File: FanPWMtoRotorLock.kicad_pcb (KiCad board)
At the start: 2 copper layers, 23 parts, among them J1 0022232031, J2 0022232031, J3 0022232031, J4 0022232031, Q1 2N2907A, Q2 2N2222A, Q3 2N2907A, Q4 2N2222A, U1 NE556

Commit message: Inital board layout work
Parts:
- removed C2: 10uf, Capacitor_THT:CP_Radial_D5.0mm_P2.50mm
- removed J3, J4: 0022232031, digikey-footprints:PinHeader_1x3_P2.54mm_Drill1.02mm
- removed Q1: 2N2907A, Package_TO_SOT_THT:TO-92
- removed Q4: 2N2222A, Package_TO_SOT_THT:TO-92
- removed R10, R11, R12, R7, R8: 10K, Resistor_THT:R_Axial_DIN0309_L9.0mm_D3.2mm_P2.54mm_Vertical
- removed R9: 100, Resistor_THT:R_Axial_DIN0309_L9.0mm_D3.2mm_P2.54mm_Vertical
- C1: footprint Capacitor_THT:CP_Radial_D5.0mm_P2.50mm -> Capacitor_SMD:C_0805_2012Metric_Pad1.18x1.45mm_HandSolder
- J2: footprint digikey-footprints:PinHeader_1x3_P2.54mm_Drill1.02mm -> Connector_JST:JST_PH_B3B-PH-K_1x03_P2.00mm_Vertical
- Q2: value 2N2222A -> MMBT2222A-7-F; footprint Package_TO_SOT_THT:TO-92 -> digikey-footprints:SOT-23-3
- Q3: value 2N2907A -> MMBT2907ALT1G; footprint Package_TO_SOT_THT:TO-92 -> digikey-footprints:SOT-23-3
- R1: footprint Resistor_THT:R_Axial_DIN0309_L9.0mm_D3.2mm_P2.54mm_Vertical -> Resistor_SMD:R_0805_2012Metric_Pad1.20x1.40mm_HandSolder; moved to B.Cu
- R2, R3, R4, R5, R6: footprint Resistor_THT:R_Axial_DIN0309_L9.0mm_D3.2mm_P2.54mm_Vertical -> Resistor_SMD:R_0805_2012Metric_Pad1.20x1.40mm_HandSolder
- U1: value NE556 -> NE555P; footprint Package_DIP:DIP-14_W7.62mm -> Package_SO:SOIC-8_3.9x4.9mm_P1.27mm; moved to B.Cu
- moved R6 86.3 mm to (129.6, 88.1), turned to 90 degrees
- moved R3 74.6 mm to (126.7, 88.1), turned to 90 degrees
- moved Q3 54.3 mm to (131.5, 83.5), turned to 0 degrees
- moved R4 49.1 mm to (129.7, 78.5), turned to 90 degrees
- moved C1 26.4 mm to (132.2, 78.5)
- moved U1 24.3 mm to (129.6, 83.2), turned to 180 degrees
- moved J2 23.5 mm to (119.0, 86.6), turned to 0 degrees
- moved J1 21.7 mm to (118.5, 80.0), turned to 0 degrees
- moved Q2 20.1 mm to (127.7, 83.5), turned to 180 degrees
- moved R5 15.7 mm to (132.4, 88.1), turned to 90 degrees
- moved R1 9.40 mm to (122.3, 82.8)
- moved R2 9.25 mm to (126.8, 78.5), turned to 90 degrees
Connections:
- C1 pad 1: Net-(Q1-C) -> Net-(Q3-E)
- C1 pad 2: Net-(Q1-E) -> Net-(Q2-E)
- J1 pad 1: Net-(Q1-E) -> Net-(Q2-E)
- J1 pad 2: Net-(U1A-R) -> Net-(U1-R)
- J2 pad 1: Net-(Q1-E) -> Net-(Q2-E)
- J2 pad 2: Net-(U1A-R) -> Net-(U1-R)
- Q2 pad 1: Net-(Q2-C) -> Net-(Q2-B)
- Q2 pad 2: Net-(Q2-B) -> Net-(Q2-E)
- Q2 pad 3: Net-(Q1-E) -> Net-(Q2-C)
- Q3 pad 1: Net-(Q3-C) -> Net-(Q3-B)
- Q3 pad 2: Net-(Q3-B) -> Net-(Q2-E)
- Q3 pad 3: Net-(Q1-E) -> Net-(Q3-E)
- R1 pad 1: Net-(U1A-R) -> Net-(U1-R)
- R2 pad 2: Net-(Q1-B) -> Net-(Q3-B)
- R3 pad 1: Net-(U1A-R) -> Net-(U1-R)
- R3 pad 2: Net-(U1A-DIS) -> Net-(U1-DIS)
- R4 pad 1: Net-(U1A-DIS) -> Net-(U1-DIS)
- R4 pad 2: Net-(Q1-C) -> Net-(Q3-E)
- R5 pad 1: Net-(U1A-Q) -> Net-(U1-Q)
- R6 pad 1: Net-(U1A-R) -> Net-(U1-R)
- U1 pad 1: Net-(U1A-DIS) -> Net-(Q2-E)
- U1 pad 2: Net-(U1A-DIS) -> Net-(Q3-B)
- U1 pad 3: unconnected-(U1A-CV-Pad3) -> Net-(U1-Q)
- U1 pad 4: Net-(U1A-R) -> Net-(U1-R)
- U1 pad 5: Net-(U1A-Q) -> unconnected-(U1-CV-Pad5)
- U1 pad 6: Net-(Q1-B) -> Net-(U1-DIS)
- U1 pad 7: Net-(Q1-E) -> Net-(U1-DIS)
- U1 pad 8: Net-(Q3-B) -> Net-(U1-R)
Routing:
- net Net-(U1-R): track 0.00 -> 30.6 mm, vias 0 -> 1
- net Net-(Q2-E): track 0.00 -> 29.7 mm, vias 0 -> 1
- net Net-(U1-DIS): track 0.00 -> 11.1 mm, vias 0 -> 2
- net Net-(Q3-B): track 0.00 -> 9.84 mm, vias 0 -> 1
- net Net-(Q2-C): track 0.00 -> 9.76 mm
- net Net-(Q3-E): track 0.00 -> 9.31 mm
- net Net-(U1-Q): track 0.00 -> 6.80 mm, vias 0 -> 1
- net Net-(J1-Pad3): track 0.00 -> 6.36 mm
- net Net-(Q2-B): track 0.00 -> 4.82 mm
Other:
- board outline added: 18.8 x 14.5 mm

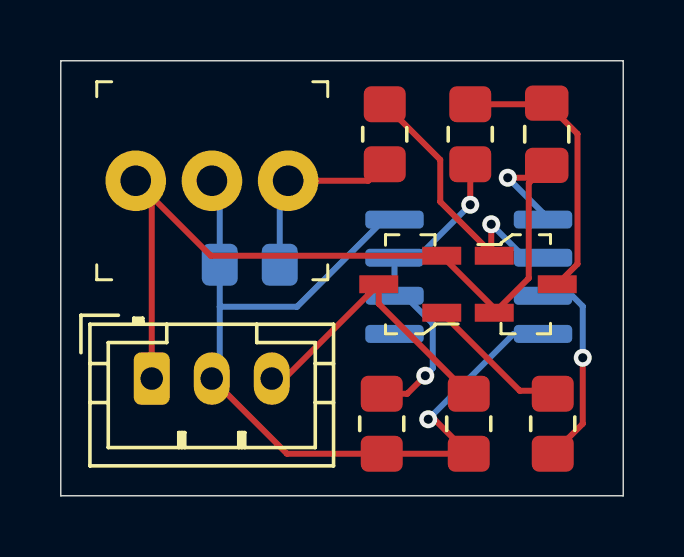
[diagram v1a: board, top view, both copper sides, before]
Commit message: Update 3D models for SOT-23 packages
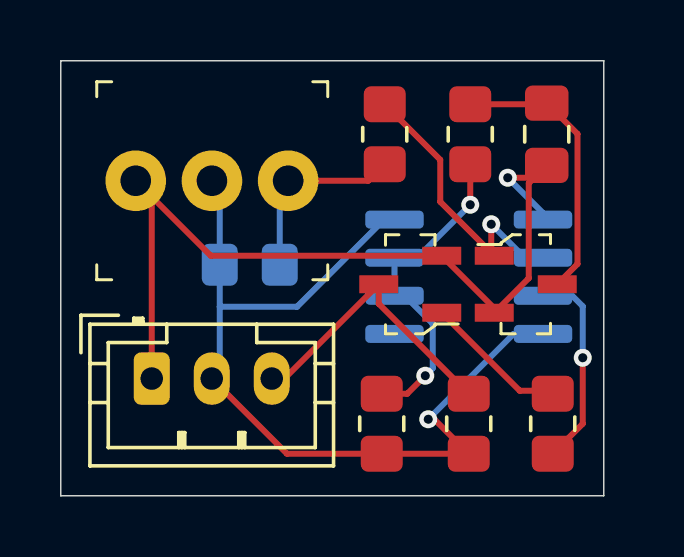
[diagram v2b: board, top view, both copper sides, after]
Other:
- board size 18.8 x 14.5 mm -> 18.1 x 14.5 mm
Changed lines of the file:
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@@
 			(outputformat 1)
 			(mirror no)
-			(drillshape 1)
+			(drillshape 0)
 			(scaleselection 1)
-			(outputdirectory "")
+			(outputdirectory "Fabrication/")
 		)
 	)
@@
 		(at 127.65 83.45 180)
 		(property "Reference" "Q2"
-			(at 0.025 -3.375 360)
+			(at 0.025 -3.375 0)
 			(layer "F.SilkS")
 			(hide yes)
@@
 		)
 		(property "Value" "MMBT2222A-7-F"
-			(at 0.025 3.25 360)
+			(at 0.025 3.25 0)
 			(layer "F.Fab")
 			(hide yes)
@@
 		)
 		(property "Footprint" "digikey-footprints:SOT-23-3"
-			(at 0 0 360)
+			(at 0 0 0)
 			(layer "F.Fab")
 			(hide yes)
@@
 		)
 		(property "Datasheet" "https://www.diodes.com/assets/Datasheets/ds30041.pdf"
-			(at 0 0 360)
+			(at 0 0 0)
 			(layer "F.Fab")
 			(hide yes)
@@
 		)
 		(property "Description" "TRANS NPN 40V 0.6A SMD SOT23-3"
-			(at 0 0 360)
+			(at 0 0 0)
 			(layer "F.Fab")
 			(hide yes)
@@
 		)
 		(fp_text user "${REFERENCE}"
-			(at -0.125 0.15 360)
+			(at -0.125 0.15 0)
 			(layer "F.Fab")
 			(effects
@@
 			(solder_mask_margin 0.07)
 		)
+		(model "${KIPRJMOD}/3DModels/MMBT2222A-7-F.step"
+			(offset
+				(xyz 0 0 0)
+			)
+			(scale
+				(xyz 1 1 1)
+			)
+			(rotate
+				(xyz -90 0 0)
+			)
+		)
 	)
 	(footprint "Resistor_SMD:R_0805_2012Metric_Pad1.20x1.40mm_HandSolder"
@@
 		(descr "http://www.molex.com/pdm_docs/sd/022232031_sd.pdf")
 		(property "Reference" "J1"
-			(at 3.71 -23.59 360)
+			(at 3.71 -23.59 0)
 			(layer "F.SilkS")
 			(hide yes)
@@
 		)
 		(property "Value" "0022232031"
-			(at 2.82 4.63 360)
+			(at 2.82 4.63 0)
 			(layer "F.Fab")
 			(hide yes)
@@
 		)
 		(property "Footprint" "digikey-footprints:PinHeader_1x3_P2.54mm_Drill1.02mm"
-			(at 0 0 360)
+			(at 0 0 0)
 			(layer "F.Fab")
 			(hide yes)
@@
 		)
 		(property "Datasheet" "https://www.molex.com/pdm_docs/sd/022232031_sd.pdf"
-			(at 0 0 360)
+			(at 0 0 0)
 			(layer "F.Fab")
 			(hide yes)
@@
 		)
 		(property "Description" "CONN HEADER VERT 3POS 2.54MM"
-			(at 0 0 360)
+			(at 0 0 0)
 			(layer "F.Fab")
 			(hide yes)
@@
 		)
 		(fp_text user "${REFERENCE}"
-			(at 2.54 0 360)
+			(at 2.54 0 0)
 			(layer "F.Fab")
 			(effects
@@
 		(at 131.5 83.45)
 		(property "Reference" "Q3"
-			(at 0.025 -3.375 360)
+			(at 0.025 -3.375 0)
 			(layer "F.SilkS")
 			(hide yes)
@@
 		)
 		(property "Value" "MMBT2907ALT1G"
-			(at 0.025 3.25 360)
+			(at 0.025 3.25 0)
 			(layer "F.Fab")
 			(hide yes)
@@
 		)
 		(property "Footprint" "digikey-footprints:SOT-23-3"
-			(at 0 0 360)
+			(at 0 0 0)
 			(layer "F.Fab")
 			(hide yes)
@@
 		)
 		(property "Datasheet" "http://www.onsemi.com/pub/Collateral/MMBT2907ALT1-D.PDF"
-			(at 0 0 360)
+			(at 0 0 0)
 			(layer "F.Fab")
 			(hide yes)
@@
 		)
 		(property "Description" "TRANS PNP 60V 0.6A SOT23"
-			(at 0 0 360)
+			(at 0 0 0)
 			(layer "F.Fab")
 			(hide yes)
@@
 		)
 		(fp_text user "${REFERENCE}"
-			(at -0.125 0.15 360)
+			(at -0.125 0.15 0)
 			(layer "F.Fab")
 			(effects
@@
 			(solder_mask_margin 0.07)
 		)
+		(model "${KIPRJMOD}/3DModels/MMBT2222A-7-F.step"
+			(offset
+				(xyz 0 0 0)
+			)
+			(scale
+				(xyz 1 1 1)
+			)
+			(rotate
+				(xyz -90 0 0)
+			)
+		)
 	)
 	(footprint "Resistor_SMD:R_0805_2012Metric_Pad1.20x1.40mm_HandSolder"
@@
 		(tags "SOIC SO")
 		(property "Reference" "U1"
-			(at 0 3.4 360)
+			(at 0 3.4 0)
 			(layer "B.SilkS")
 			(hide yes)
@@
 		)
 		(property "Value" "NE555P"
-			(at 0 -3.4 360)
+			(at 0 -3.4 0)
 			(layer "B.Fab")
 			(hide yes)
@@
 		)
 		(property "Footprint" "Package_SO:SOIC-8_3.9x4.9mm_P1.27mm"
-			(at 0 0 360)
+			(at 0 0 0)
 			(layer "B.Fab")
 			(hide yes)
@@
 		)
 		(property "Datasheet" "http://www.ti.com/lit/ds/symlink/ne555.pdf"
-			(at 0 0 360)
+			(at 0 0 0)
 			(layer "B.Fab")
 			(hide yes)
@@
 		)
 		(property "Description" "Precision Timers, 555 compatible,  PDIP-8"
-			(at 0 0 360)
+			(at 0 0 0)
 			(layer "B.Fab")
 			(hide yes)
@@
 		)
 		(fp_text user "${REFERENCE}"
-			(at 0 0 360)
+			(at 0 0 0)
 			(layer "B.Fab")
 			(effects
@@
 		(tags "resistor handsolder")
 		(property "Reference" "R1"
-			(at 0 1.65 360)
+			(at 0 1.65 0)
 			(layer "B.SilkS")
 			(hide yes)
@@
 		)
 		(property "Value" "10K"
-			(at 0 -1.65 360)
+			(at 0 -1.65 0)
 			(layer "B.Fab")
 			(hide yes)
@@
 		)
 		(fp_text user "${REFERENCE}"
-			(at 0 0 360)
+			(at 0 0 0)
 			(layer "B.Fab")
 			(effects
@@
 	(gr_rect
 		(start 116 76)
-		(end 134.75 90.5)
+		(end 134.1 90.5)
 		(stroke
 			(width 0.05)

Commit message: Final layout, ready for manufacture
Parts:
- R2, R6: moved to B.Cu
- moved R5 16.0 mm to (116.4, 86.9), turned to -90 degrees
- moved U1 10.7 mm to (119.4, 86.4), turned to 0 degrees
- moved J2 9.72 mm to (126.1, 79.9)
- moved R4 9.07 mm to (127.1, 87.2), turned to -90 degrees
- moved Q2 8.45 mm to (120.0, 87.0)
- moved Q3 8.24 mm to (124.1, 87.1), turned to -90 degrees
- moved R2 7.05 mm to (124.9, 85.2), turned to -90 degrees
- moved C1 6.28 mm to (130.5, 84.5), turned to 0 degrees
- moved R1 5.57 mm to (127.3, 85.2), turned to -90 degrees
- moved R3 3.80 mm to (130.5, 88.0), turned to 180 degrees
- moved R6 2.85 mm to (129.6, 85.2)
- moved J1 2.06 mm to (116.8, 81.1)
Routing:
- net Net-(U1-R): track 30.6 -> 41.2 mm, vias 1 -> 0
- net Net-(Q2-C): track 9.76 -> 19.2 mm
- net Net-(Q2-E): track 29.7 -> 36.4 mm, vias 1 -> 0
- net Net-(U1-Q): track 6.80 -> 3.48 mm
- net Net-(Q3-B): track 9.84 -> 12.0 mm
- net Net-(U1-DIS): track 11.1 -> 12.5 mm, vias 2 -> 1
- net Net-(J1-Pad3): track 6.36 -> 7.60 mm
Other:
- board size 18.1 x 14.5 mm -> 17.7 x 12 mm

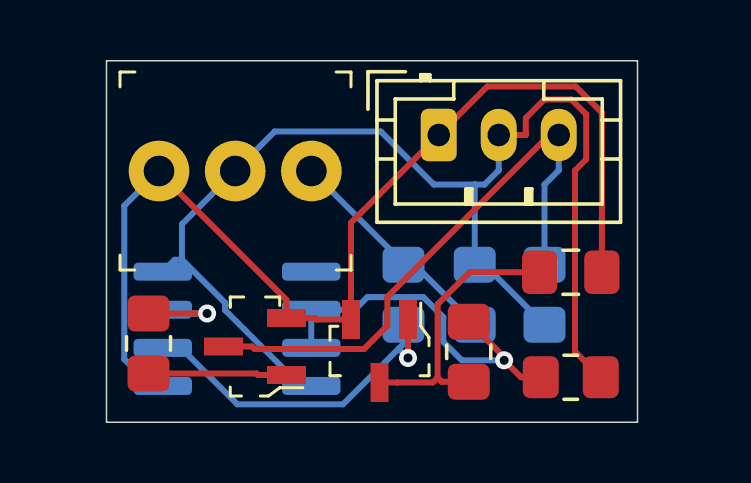
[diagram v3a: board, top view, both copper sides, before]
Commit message: Added decoupling cap, shrunk board layout
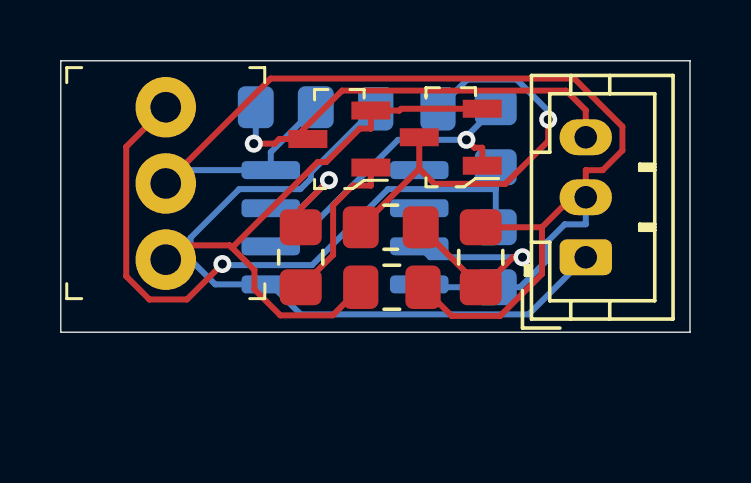
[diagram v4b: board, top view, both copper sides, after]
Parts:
- added C2: .1uf, Capacitor_SMD:C_0805_2012Metric_Pad1.18x1.45mm_HandSolder, F.Cu at (124.5, 85.0)
- C1: moved to B.Cu
- moved R6 10.7 mm to (121.0, 79.0), turned to 180 degrees
- moved C1 7.71 mm to (125.0, 79.1), turned to 180 degrees
- moved Q3 7.51 mm to (126.5, 80.0), turned to 180 degrees
- moved Q2 7.46 mm to (122.8, 80.1)
- moved J2 6.37 mm to (131.0, 84.0), turned to 90 degrees
- moved R2 6.08 mm to (128.0, 80.0), turned to 90 degrees
- moved R5 5.83 mm to (121.5, 84.0)
- moved R3 5.00 mm to (127.5, 84.0), turned to -90 degrees
- moved U1 4.94 mm to (123.0, 83.0)
- moved R4 4.90 mm to (124.5, 83.0), turned to 180 degrees
- moved J1 2.96 mm to (117.0, 84.1), turned to 90 degrees
- moved R1 1.43 mm to (128.0, 84.0), turned to 90 degrees
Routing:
- net Net-(J1-Pad3): track 7.60 -> 22.4 mm, vias 0 -> 1
- net Net-(Q2-E): track 36.4 -> 43.4 mm
- net Net-(Q3-E): track 9.39 -> 14.4 mm, vias 0 -> 1
- net Net-(Q2-C): track 19.2 -> 14.7 mm, vias 0 -> 1
- net Net-(U1-R): track 41.2 -> 45.1 mm
- net Net-(U1-DIS): track 12.5 -> 9.61 mm
- net Net-(Q3-B): track 12.0 -> 10.7 mm
- net Net-(U1-Q): track 3.48 -> 4.28 mm
- net Net-(Q2-B): track 4.62 -> 5.31 mm
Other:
- board size 17.7 x 12 mm -> 21 x 9 mm
